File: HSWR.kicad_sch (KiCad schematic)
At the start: 21 parts, among them J1 USB_B, J2 IO, J3 B+, J4 B-, J5 U, J6 V, J7 W

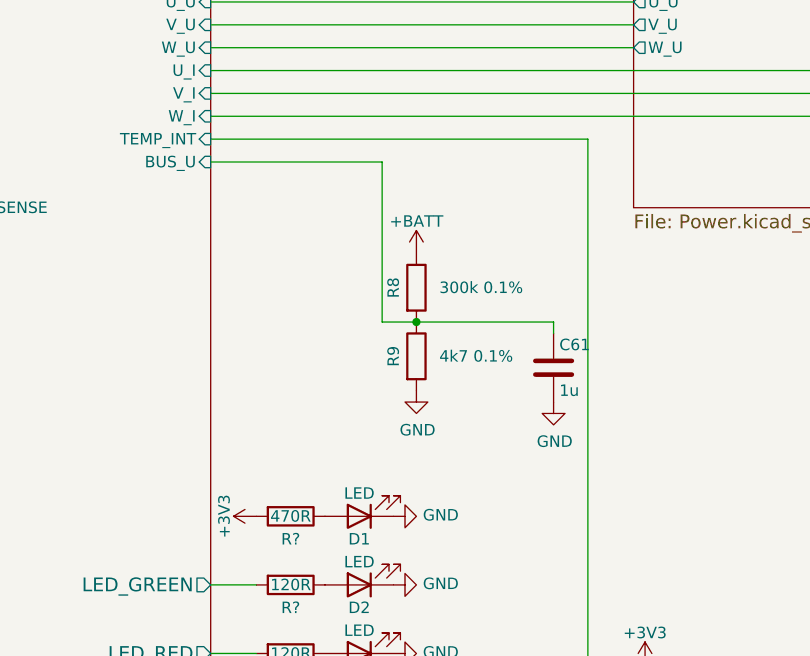
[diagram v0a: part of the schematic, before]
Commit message: HSWR V4.1: - added opamp for better voltage measurement
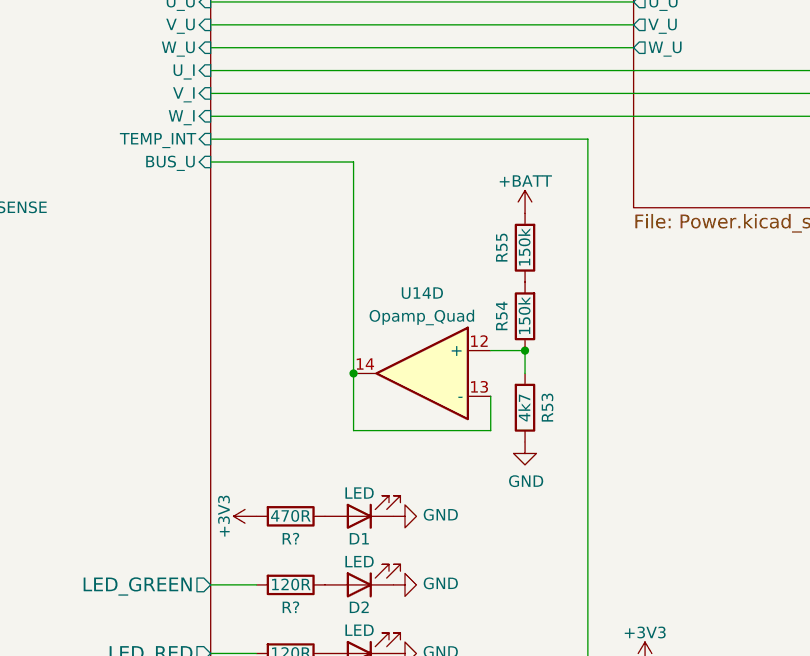
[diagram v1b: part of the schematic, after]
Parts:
- removed C61: 1u, Capacitor_SMD:C_0805_2012Metric, symbol Device:C
- removed R8: 300k 0.1%, Resistor_SMD:R_0805_2012Metric, symbol Device:R
- removed R9: 4k7 0.1%, Resistor_SMD:R_0805_2012Metric, symbol Device:R
- added R53: 4k7, Resistor_SMD:R_0805_2012Metric, symbol Device:R
- added R54, R55: 150k, Resistor_SMD:R_0805_2012Metric, symbol Device:R
- added U14: Opamp_Quad, Package_SO:SO-14_3.9x8.65mm_P1.27mm, symbol Device:Opamp_Quad
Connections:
- net +BATT: now also R55.2
- net GND: now also R53.1
- net MCU/BUS_U: now also U14.13 (-), U14.14
- new net: R54.2, R55.1
- new net: R53.2, R54.1, U14.12 (+)

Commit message: - some work on schematic
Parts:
- added J10: W2, MountingHole:MountingHole_6.5mm_Pad_Via, symbol HSWR-rescue:Conn_01x01_Male-Connector
- added J8: U2, MountingHole:MountingHole_6.5mm_Pad_Via, symbol HSWR-rescue:Conn_01x01_Male-Connector
- added J9: V2, MountingHole:MountingHole_6.5mm_Pad_Via, symbol HSWR-rescue:Conn_01x01_Male-Connector
- J5: value U -> U1
- J6: value V -> V1
- J7: value W -> W1
- renumbered D4 to D1, D3 to D2, D2 to D3, D1 to D4, J2 to J1, J1 to J2
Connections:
- new net Power MOSFETS 2/U: J8.1 (Pin_1)
- new net Power MOSFETS 2/V: J9.1 (Pin_1)
- new net Power MOSFETS 2/W: J10.1 (Pin_1)
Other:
- sheet Mosfet driver renamed Mosfet driver 1
- sheet Power MOSFETS renamed Power MOSFETS 1
- added sheet Mosfet driver 2 (Power2.kicad_sch)
- added sheet Power MOSFETS 2 (mosfets2.kicad_sch)
- sheet MCU ports: added H1_1, H1_2, H1_3, H2_1, H2_2, H2_3, U1_I, U1_PWM_H, U1_PWM_L, U1_U, U2_I, U2_PWM_H, U2_PWM_L, U2_U, V1_PWM_H, V1_PWM_L, V1_U, V2_PWM_H, V2_PWM_L, V2_U, W1_I, W1_PWM_H, W1_PWM_L, W1_U, W2_I, W2_PWM_H, W2_PWM_L, W2_U; removed HALL_1, HALL_2, HALL_3, U_I, U_PWM_H, U_PWM_L, U_U, V_I, V_PWM_H, V_PWM_L, V_U, W_I, W_PWM_H, W_PWM_L, W_U
- sheet Mosfet driver 1: file Power.kicad_sch -> Power1.kicad_sch
- sheet Power MOSFETS 1: file mosfets.kicad_sch -> mosfets1.kicad_sch
- sheet Power MOSFETS 1 ports: added none; removed V_I
- note added: "HSWR DUAL V1 200V+ 100A"
- note removed: "HSWR V4 200V 100A"
- title: HSWR.0 200V 50A -> HSWR_DUAL V1
- moved on the sheet: C1, D2, D3, D4, J5, J6, J7, R53, R54, R55, R?, U14D

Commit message: - some layout work
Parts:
- added J13: CAN, Connector_Phoenix_MC:PhoenixContact_MCV_1,5_4-G-3.5_1x04_P3.50mm_Vertical, symbol Connector:Conn_01x04_Pin
- added J14: Motor1, Connector_Phoenix_MC:PhoenixContact_MCV_1,5_6-G-3.5_1x06_P3.50mm_Vertical, symbol Connector:Conn_01x06_Pin
- added J15: FAN, Connector_Phoenix_MC:PhoenixContact_MCV_1,5_2-G-3.5_1x02_P3.50mm_Vertical, symbol Connector:Conn_01x02_Pin
- J1: value IO -> Motor1; footprint Connector_IDC:IDC-Header_2x08_P2.54mm_Vertical_Lock -> Connector_Phoenix_MC:PhoenixContact_MCV_1,5_6-G-3.5_1x06_P3.50mm_Vertical; symbol HSWR-rescue:Conn_01x16_Male-Connector -> Connector:Conn_01x06_Pin
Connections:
- net iso IO/Hall_1B is gone; now on net Earth: J1.6 (Pin_6)
- net +12VA: now also J1.1 (Pin_1), J14.1 (Pin_1), J15.1 (Pin_1); no longer J1.14 (Pin_14)
- net CAN bus transceiver/CANH: now also J13.2 (Pin_2); no longer J1.2 (Pin_2)
- net CAN bus transceiver/CANL: now also J13.3 (Pin_3); no longer J1.3 (Pin_3)
- net Earth: now also J13.4 (Pin_4), J14.6 (Pin_6); no longer J1.16 (Pin_16), J1.4 (Pin_4)
- net iso IO/Fan_Out: now also J15.2 (Pin_2); no longer J1.15 (Pin_15)
- net at F1.2: now also J13.1 (Pin_1); no longer J1.1 (Pin_1)
- net iso IO/Hall_1A renamed iso IO/M1_Temp
- removed net iso IO/Hall_2A: J1.7 (Pin_7)
- removed net iso IO/Hall_2B: J1.8 (Pin_8)
- removed net iso IO/Hall_3A: J1.9 (Pin_9)
- removed net iso IO/Hall_3B: J1.10 (Pin_10)
- removed net iso IO/M_Temp: J1.13 (Pin_13)
- removed net iso IO/UART_A: J1.11 (Pin_11)
- removed net iso IO/UART_B: J1.12 (Pin_12)
- new net iso IO/Hall1_A: J1.2 (Pin_2)
- new net iso IO/Hall1_B: J1.3 (Pin_3)
- new net iso IO/Hall1_C: J1.4 (Pin_4)
- new net iso IO/Hall2_A: J14.2 (Pin_2)
- new net iso IO/Hall2_B: J14.3 (Pin_3)
- new net iso IO/Hall2_C: J14.4 (Pin_4)
- new net iso IO/M2_Temp: J14.5 (Pin_5)
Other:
- sheet iso IO ports: added Fan, H1_A, H1_B, H1_C, H2_A, H2_B, H2_C, Hall1_A, Hall1_B, Hall1_C, Hall2_A, Hall2_B, Hall2_C, M1_Temp, M2_Temp; removed Fan_In, Hall_1, Hall_1A, Hall_1B, Hall_2, Hall_2A, Hall_2B, Hall_3, Hall_3A, Hall_3B, M_Temp, UART_A, UART_B
- moved on the sheet: D1, F1, J2

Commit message: - layout almost finished
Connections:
- net Power MOSFETS 1/U renamed Power MOSFETS 1/U1
- net Power MOSFETS 1/V renamed Power MOSFETS 1/V1
- net Power MOSFETS 1/W renamed Power MOSFETS 1/W1
- net Power MOSFETS 2/U renamed U2
- net Power MOSFETS 2/V renamed V2
- net Power MOSFETS 2/W renamed W2
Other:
- sheet Mosfet driver 1 ports: added U1_GH, U1_GL, U1_PWM_H, U1_PWM_L, U1_U, U1_VP, V1_GH, V1_GL, V1_PWM_H, V1_PWM_L, V1_U, V1_VP, W1_GH, W1_GL, W1_PWM_H, W1_PWM_L, W1_U, W1_VP; removed U_GH, U_GL, U_PWM_H, U_PWM_L, U_U, U_VP, U_VS, V_GH, V_GL, V_PWM_H, V_PWM_L, V_U, V_VP, V_VS, W_GH, W_GL, W_PWM_H, W_PWM_L, W_U, W_VP, W_VS
- sheet Mosfet driver 2 ports: added U2_GH, U2_GL, U2_PWM_H, U2_PWM_L, U2_U, U2_VP, V2_GH, V2_GL, V2_PWM_H, V2_PWM_L, V2_U, V2_VP, W2_GH, W2_GL, W2_PWM_H, W2_PWM_L, W2_U, W2_VP; removed U_GH, U_GL, U_PWM_H, U_PWM_L, U_U, U_VP, U_VS, V_GH, V_GL, V_PWM_H, V_PWM_L, V_U, V_VP, V_VS, W_GH, W_GL, W_PWM_H, W_PWM_L, W_U, W_VP, W_VS
- sheet Power MOSFETS 1 ports: added U1, U1_GH, U1_GL, U1_I, U1_VP, V1, V1_GH, V1_GL, V1_I, V1_VP, W1, W1_GH, W1_GL, W1_VP; removed U, U_GH, U_GL, U_I, U_VP, U_VS, V, V_GH, V_GL, V_VP, V_VS, W, W_GH, W_GL, W_I, W_VP, W_VS
- sheet Power MOSFETS 2 ports: added U2, U2_GH, U2_GL, U2_I, U2_VP, V2, V2_GH, V2_GL, V2_I, V2_VP, W2, W2_GH, W2_GL, W2_VP; removed U, U_GH, U_GL, U_I, U_VP, U_VS, V, V_GH, V_GL, V_VP, V_VS, W, W_GH, W_GL, W_I, W_VP, W_VS

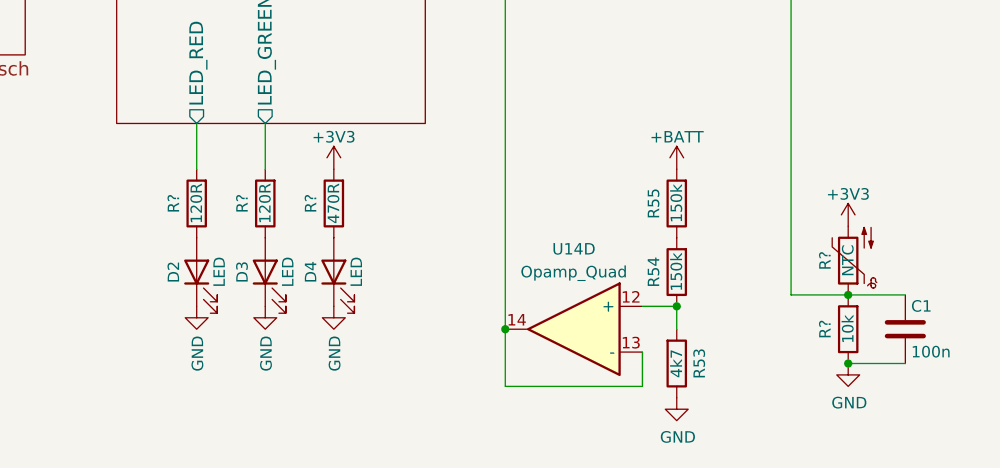
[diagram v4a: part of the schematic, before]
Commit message: - fixed missing 3V3 trace on USB isolator
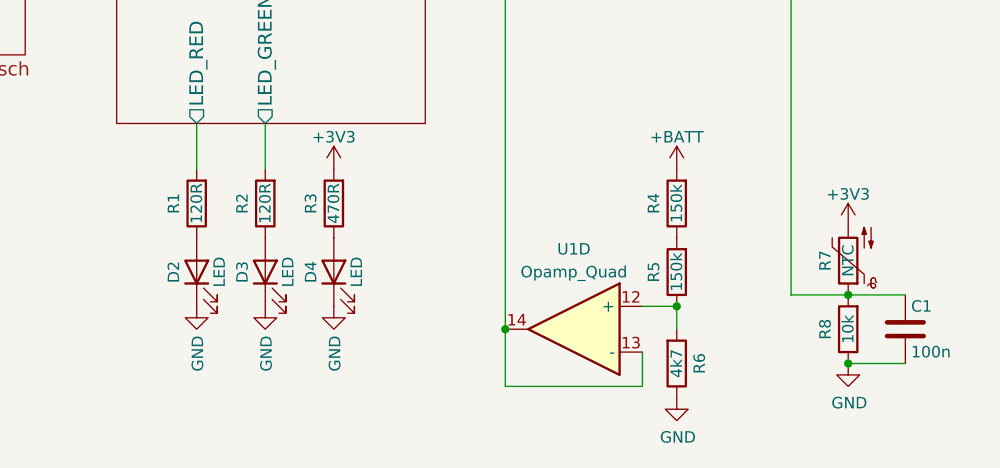
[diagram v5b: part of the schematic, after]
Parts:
- gave numbers to parts that had none: 5
- renumbered R55 to R4, R54 to R5, R53 to R6, U14 to U1
